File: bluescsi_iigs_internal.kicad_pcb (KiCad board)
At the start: 2 copper layers, 56.6 x 53.3 mm, 16 parts, among them J1 Conn_02x13_Odd_Even, J2 Conn_02x13_Odd_Even, J3 Micro_SD_Card, SW1 SW_SPDT, U1 YAAJ_BluePill, U2 UCC5606, U3 UCC5606

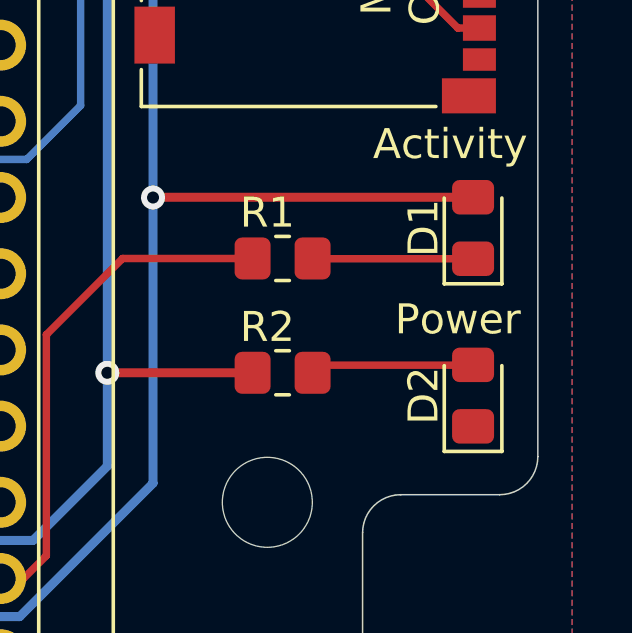
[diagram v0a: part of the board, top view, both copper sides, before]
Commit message: nudge leds, add groind vias
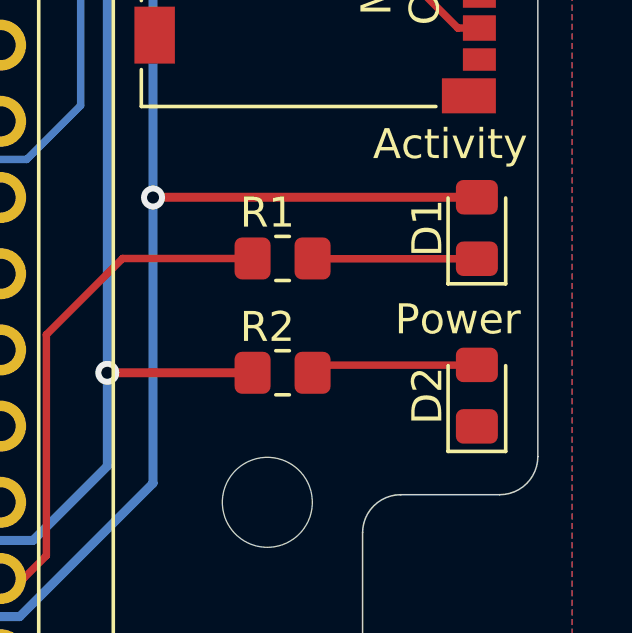
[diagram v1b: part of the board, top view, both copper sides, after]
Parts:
- moved D1 0.13 mm to (183.5, 84.8)
- moved D2 0.13 mm to (183.5, 90.4)
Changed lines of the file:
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@@
   )
   (module LED_SMD:LED_0805_2012Metric_Pad1.15x1.40mm_HandSolder (layer F.Cu)
-    (at 183.388 90.424 90)
+    (at 183.515 90.424 90)
     (descr "LED SMD 0805 (2012 Metric), square (rectangular) end terminal, IPC_7351 nominal, (Body size source: https://docs.google.com/spreadsheets/d/1BsfQQcO9C6DZCsRaXUlFlo91Tg2WpOkGARC1WS5S8t0/edit?usp=sharing), generated with kicad-footprint-generator")
     (tags "LED handsolder")
@@
   )
   (module LED_SMD:LED_0805_2012Metric_Pad1.15x1.40mm_HandSolder (layer F.Cu)
-    (at 183.388 84.836 90)
+    (at 183.515 84.836 90)
     (descr "LED SMD 0805 (2012 Metric), square (rectangular) end terminal, IPC_7351 nominal, (Body size source: https://docs.google.com/spreadsheets/d/1BsfQQcO9C6DZCsRaXUlFlo91Tg2WpOkGARC1WS5S8t0/edit?usp=sharing), generated with kicad-footprint-generator")
     (tags "LED handsolder")
@@
   (segment (start 171.196 58.42) (end 171.196 89.662) (width 0.3) (layer B.Cu) (net 12))
   (via (at 171.196 58.42) (size 0.8) (drill 0.4) (layers F.Cu B.Cu) (net 12))
+  (segment (start 159.02532 62.233641) (end 164.108961 57.15) (width 0.3) (layer F.Cu) (net 12))
+  (segment (start 164.108961 57.15) (end 169.926 57.15) (width 0.3) (layer F.Cu) (net 12))
+  (segment (start 169.926 57.15) (end 172.248 59.472) (width 0.3) (layer F.Cu) (net 12))
   (segment (start 172.248 59.472) (end 180.942 59.472) (width 0.3) (layer F.Cu) (net 12))
-  (segment (start 169.926 57.15) (end 172.248 59.472) (width 0.3) (layer F.Cu) (net 12))
-  (segment (start 164.108961 57.15) (end 169.926 57.15) (width 0.3) (layer F.Cu) (net 12))
-  (segment (start 159.02532 62.233641) (end 164.108961 57.15) (width 0.3) (layer F.Cu) (net 12))
   (via (at 155.448 86.233) (size 0.8) (drill 0.4) (layers F.Cu B.Cu) (net 13))
   (segment (start 155.575 85.725) (end 155.067 86.233) (width 0.25) (layer B.Cu) (net 13))
@@
   (segment (start 169.672 64.77) (end 165.1 64.77) (width 0.25) (layer B.Cu) (net 43))
   (segment (start 170.307 65.405) (end 169.672 64.77) (width 0.25) (layer B.Cu) (net 43))
+  (segment (start 180.942 60.972) (end 170.803 60.972) (width 0.25) (layer F.Cu) (net 43))
   (segment (start 170.307 61.468) (end 170.307 65.405) (width 0.25) (layer F.Cu) (net 43))
   (segment (start 170.803 60.972) (end 170.307 61.468) (width 0.25) (layer F.Cu) (net 43))
-  (segment (start 180.942 60.972) (end 170.803 60.972) (width 0.25) (layer F.Cu) (net 43))
   (segment (start 178.047 85.861) (end 183.388 85.861) (width 0.25) (layer F.Cu) (net 44) (status 30))
   (segment (start 178.038 85.852) (end 178.047 85.861) (width 0.25) (layer F.Cu) (net 44) (status 30))

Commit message: nudge the switch out a little, since ground can still pass underneath it
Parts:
- moved SW1 0.51 mm to (182.9, 61.7)
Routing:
- net +5V: track 116.7 -> 116.1 mm
- net GND: vias 4 -> 6

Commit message: Add auxilliary 12v input
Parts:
- added C4: 10uF, Capacitor_Tantalum_SMD:CP_EIA-3528-21_Kemet-B_Pad1.50x2.35mm_HandSolder, B.Cu at (136.1, 96.0)
- added D3: 1N5817, Diode_SMD:D_MicroMELF, F.Cu at (145.8, 98.0)
- added D4: 1N5817, Diode_SMD:D_MicroMELF, F.Cu at (145.8, 94.5)
- added J4: Conn_01x02_Male, Connector_PinHeader_2.54mm:PinHeader_1x02_P2.54mm_Vertical, F.Cu at (131.1, 95.8)
- added U4: AMS1117-5.0, Package_TO_SOT_SMD:SOT-223-3_TabPin2, F.Cu at (138.2, 96.5)
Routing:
- net Net-(D3-Pad2): track 0.00 -> 10.6 mm
- net Net-(D4-Pad2): track 0.00 -> 10.1 mm
- net /+12V_AUX: track 0.00 -> 9.40 mm
- net +5V: track 116.1 -> 123.6 mm
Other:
- board text added: "Aux +12V Power In"
- board text added: "For Apple Rev. C SCSI card, and cards with compatible IDC26-DB25 connector pinout"
- board text removed: "For Apple Rev. C SCSI card w/ termination power modification, and cards with compatible IDC26-DB25 connector pinout"

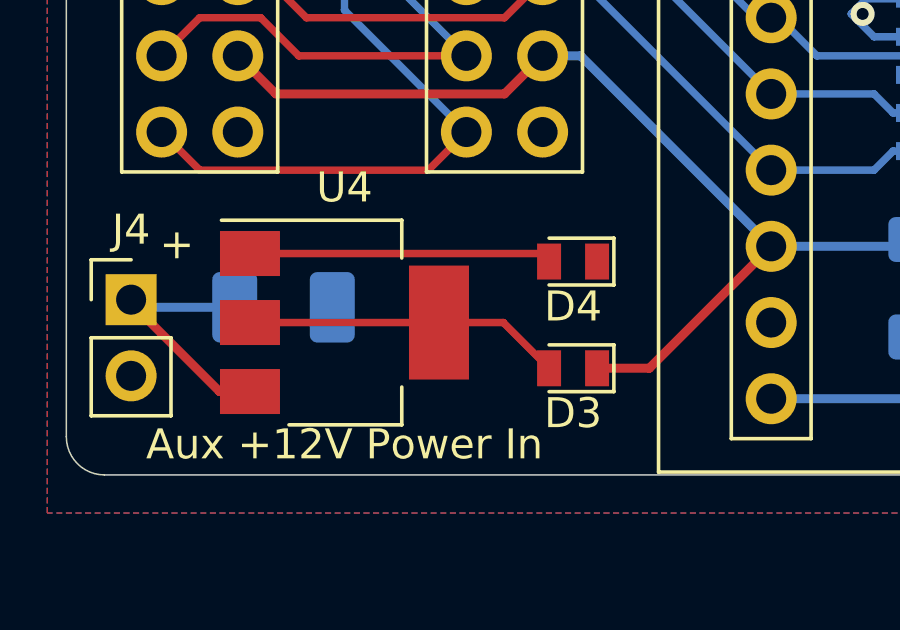
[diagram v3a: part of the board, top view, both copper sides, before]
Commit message: Change footprint of diodes
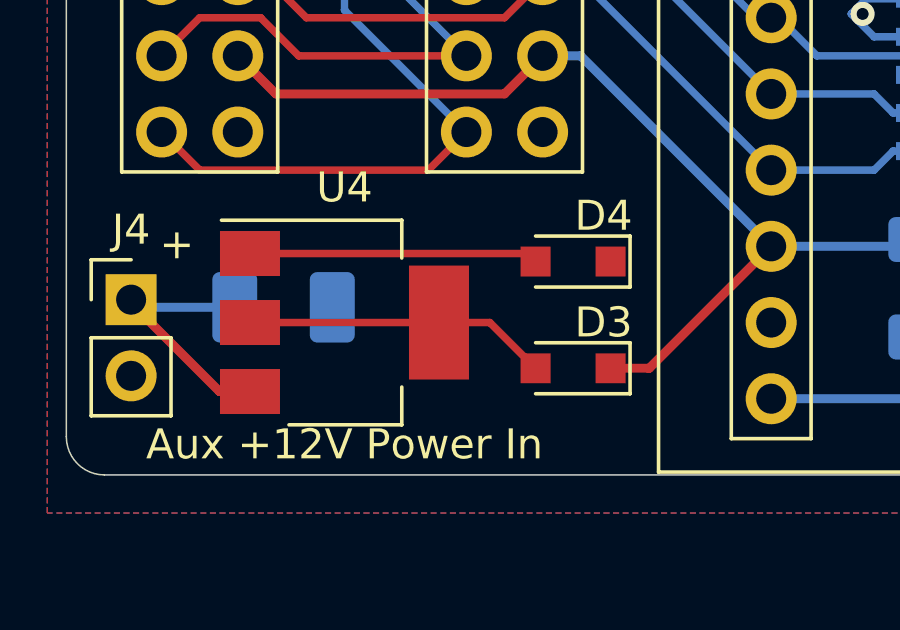
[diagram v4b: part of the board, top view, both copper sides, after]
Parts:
- D3: value 1N5817 -> 1N5817,1N5817,CUS08F30-H3F; footprint Diode_SMD:D_MicroMELF -> Diode_SMD:D_SOD-323_HandSoldering
- D4: value 1N5817 -> 1N5817,CUS08F30-H3F; footprint Diode_SMD:D_MicroMELF -> Diode_SMD:D_SOD-323_HandSoldering

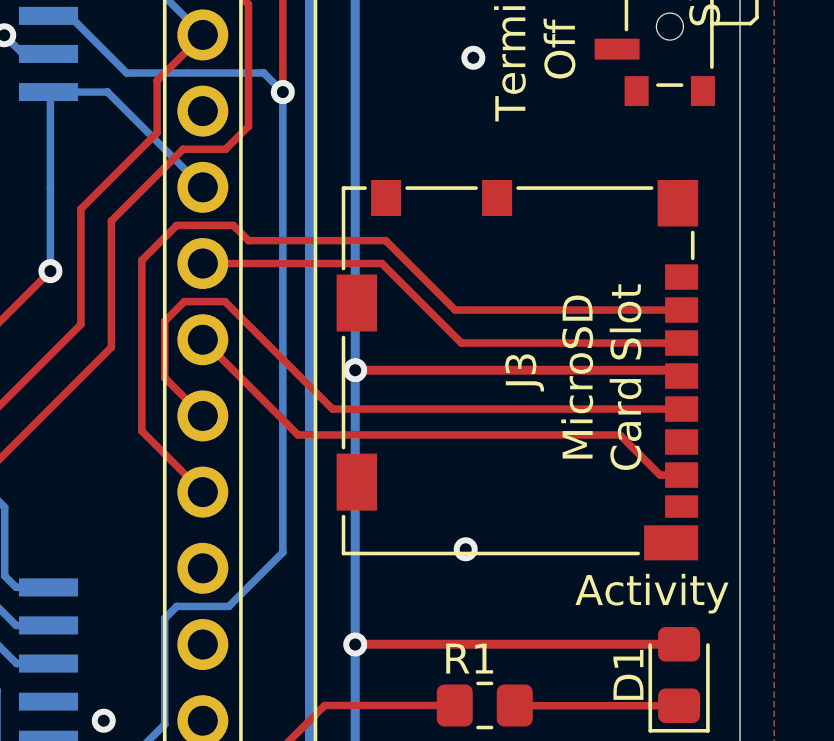
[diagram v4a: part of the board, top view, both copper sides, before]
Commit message: Remove UCC5606 from rear silk since will make this compatible with other ICs in future
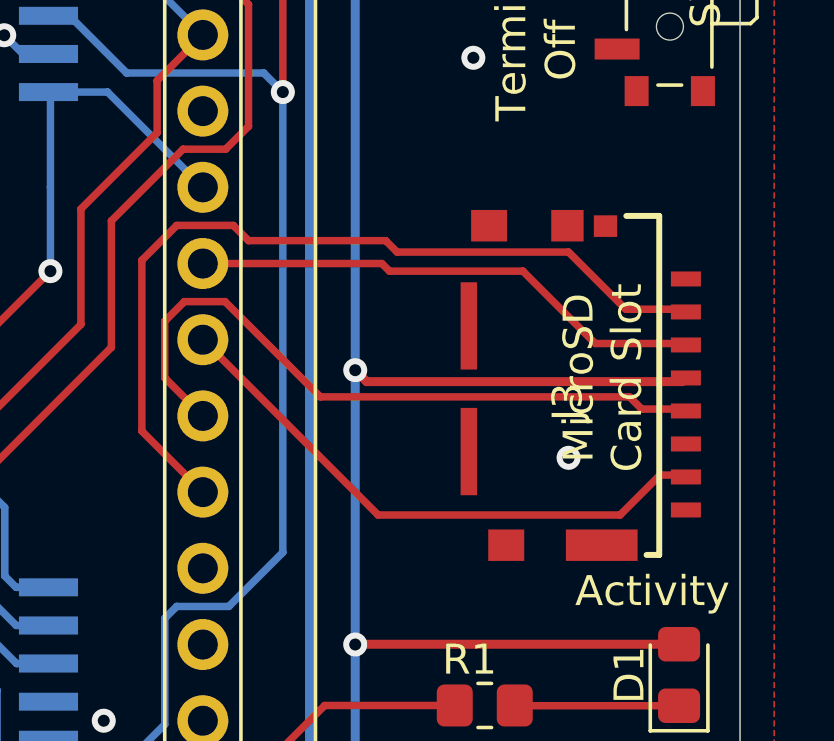
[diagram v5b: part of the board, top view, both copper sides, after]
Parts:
- J3: value Micro_SD_Card -> 105162-0001; footprint Connector_Card:microSD_HC_Molex_104031-0811 -> Molex 105162-0001:105162-0001
- moved J3 1.82 mm to (176.4, 75.2), turned to 90 degrees
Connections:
- J3 pad 10: (no net) -> GND
- J3 pad 11: (no net) -> GND
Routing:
- net /SD_MISO: track 18.0 -> 19.1 mm
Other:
- board text added: "Apple IIGS and //e Internal BlueSCSI v1.2 - May 2021"
- board text removed: "UCC5606"
